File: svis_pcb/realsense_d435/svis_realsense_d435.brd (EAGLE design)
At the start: 57.1 x 41.3 mm, 14 parts, among them U1 MPU-6000QFN-24

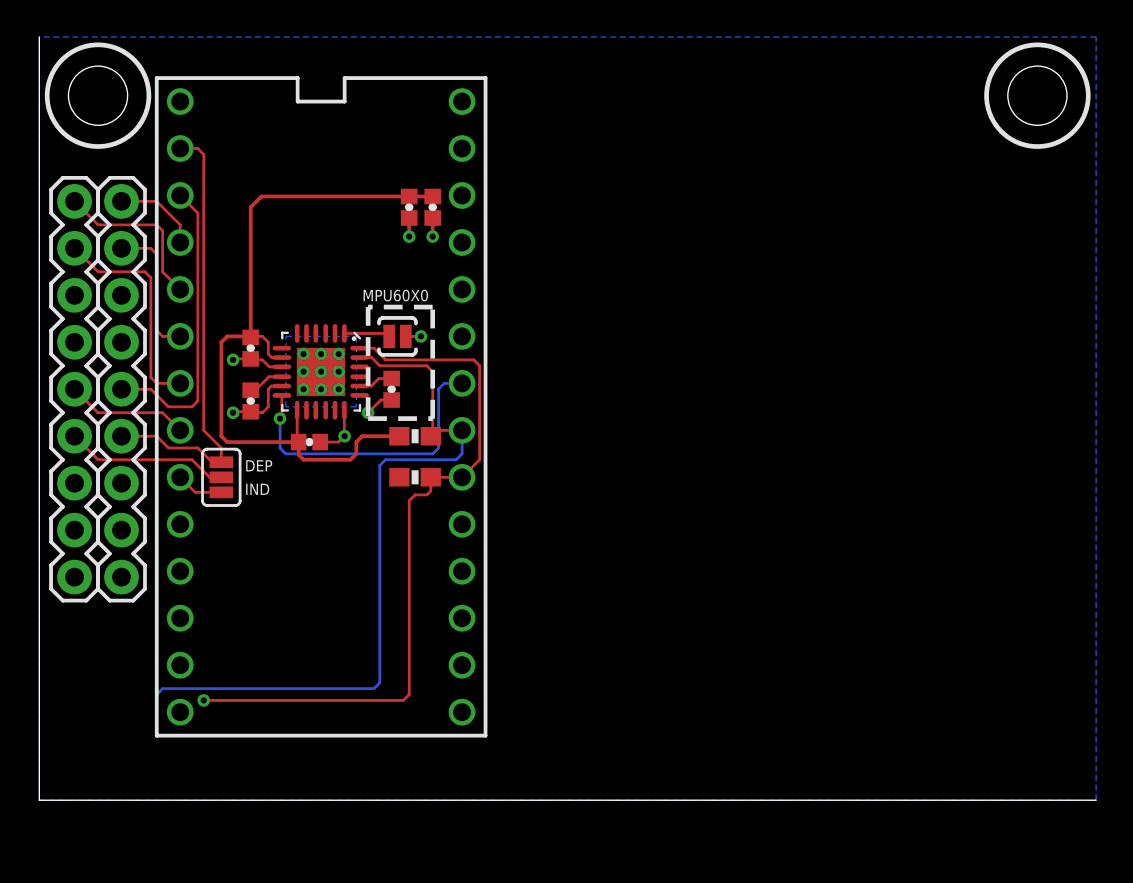
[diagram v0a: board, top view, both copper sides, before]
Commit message: Adding libraries and packages.
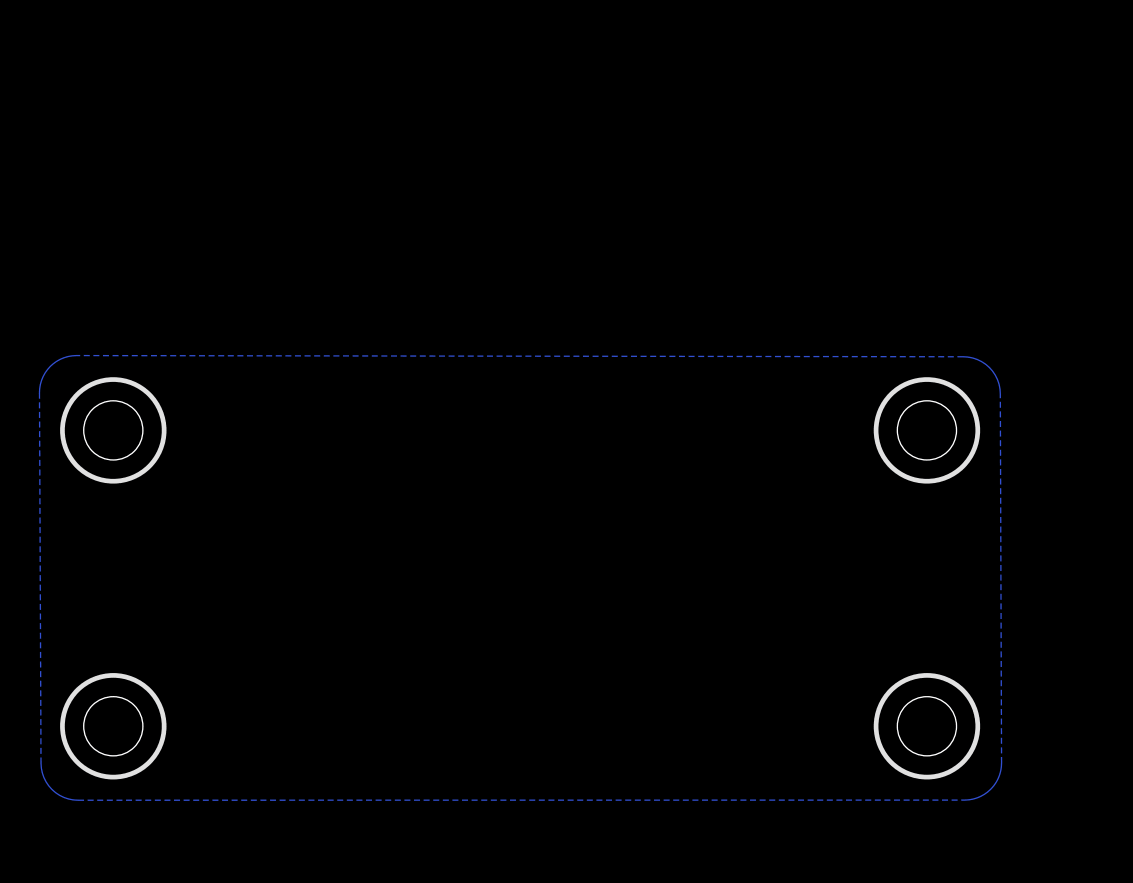
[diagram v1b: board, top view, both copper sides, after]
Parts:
- removed C1: DNP (2.2nF), SparkFun-Capacitors:0402-CAP
- removed C2, C3, C5, C6: 0.1uF, SparkFun-Capacitors:0402-CAP
- removed C4: 2.2uF, SparkFun-Capacitors:0402-CAP
- removed J2, J3: (no value), SparkFun-Connectors:1X09
- removed JP1: MPU6050, SparkFun-Passives:PAD-JUMPER-2-NO_YES_SILK
- removed JP2: JUMPER-SMT_3_NO_SILK, SparkFun-Jumpers:SMT-JUMPER_3_NO_SILK
- removed R1, R2: 4.7k, SparkFun-Resistors:0603-RES
- removed U$2: TEENSY_3.2, Teensy_3_and_LC_Series_Boards_v1.1:TEENSY3-DIL
- removed U1: MPU-6000QFN-24, SparkFun-Sensors:QFN-24-TESTING
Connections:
- removed net 3.3V: C3.1, C4.1, C5.1, C6.1, R1.2, R2.2, U$2.3.3V, U1.13, U1.8
- removed net C31_I0: J2.9, U$2.2
- removed net C31_IO2_RX: J2.5, U$2.1
- removed net C31_IO3_TX: J2.4, JP2.1, U$2.0
- removed net C31_O1: J2.8, U$2.4
- removed net C32_I0: J3.9, U$2.3
- removed net C32_IO2: J3.5, U$2.6
- removed net C32_IO3: J3.4, JP2.2
- removed net C32_IO3_T: JP2.3, U$2.7
- removed net C32_O1: J3.8, U$2.5
- removed net GND: C1.1, C2.1, C3.2, C4.2, C5.2, C6.2, J2.2, J2.6, J2.7, J3.2, J3.6, J3.7, JP1.1, U$2.AGND, U$2.GND, U1.11, U1.18, U1.9
- removed net IMU2_INT: U$2.20/A6, U1.12
- removed net N$7: C1.2, U1.20
- removed net N$8: JP1.2, U1.1
- removed net REGOUT: C2.2, U1.10
- removed net SCL: R1.1, U$2.19/A5, U1.23
- removed net SDA: R2.1, U$2.18/A4, U1.24
- removed net VIN: U$2.VIN
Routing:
- net 3.3V: track 39.8 -> 0.00 mm
- net SCL: track 39.6 -> 0.00 mm
- net SDA: track 38.8 -> 0.00 mm, vias 1 -> 0
- net C31_IO3_TX: track 24.4 -> 0.00 mm
- net IMU2_INT: track 16.3 -> 0.00 mm, vias 1 -> 0
- net C31_IO2_RX: track 16.2 -> 0.00 mm
- net GND: track 14.0 -> 0.00 mm, vias 7 -> 0
- net C32_O1: track 11.9 -> 0.00 mm
- net C32_I0: track 8.99 -> 0.00 mm
- net C32_IO3: track 8.86 -> 0.00 mm
- net C31_O1: track 7.57 -> 0.00 mm
- net C32_IO2: track 6.64 -> 0.00 mm
- net C31_I0: track 4.65 -> 0.00 mm
- net C32_IO3_T: track 2.56 -> 0.00 mm
- net N$8: track 2.49 -> 0.00 mm
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- removed copper zone on layer 16, net HS
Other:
- board outline removed
- board text removed: "DEP"
- board text removed: "IND"
- board text removed: "MPU60X0"

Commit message: WIP.
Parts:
- added C1: 0.1uF, SparkFun-Capacitors:0402
- added U$1: TEENSY_3.0_DIL, teensy:TEENSY_3.0-3.2&LC_DIL
- added U1: ICM-20689, svis:QFN50P400X400X95-25N
- added U2: SM09B-SRSS-TB, svis:SM09B-SRSS-TB
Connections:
- new net 3.3V: U$1.3.3V, U1.13, U1.8
- new net GND: C1.1, U$1.AGND, U$1.GND, U1.11, U1.18, U1.25
- new net IMU_INT: U1.12
- new net N$1: C1.2, U1.10
- new net VIN: U$1.VIN

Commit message: First cut at complete board.
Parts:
- added C2: 0.1uF, SparkFun-Capacitors:0603
- added C3: 2.2uF, SparkFun-Capacitors:0603
- added C4: 10nF, SparkFun-Capacitors:0603
- added CAM2: SM09B-SRSS-TB, svis:SM09B-SRSS-TB
- added R1, R2: 4.7k, SparkFun-Resistors:0603
- C1: value 0.1uF -> 0.47uF; device SparkFun-Capacitors:0402 -> SparkFun-Capacitors:0603
- moved C1 24.0 mm to (24.0, 7.50), flipped to the bottom
- renumbered U$1 to TEENSY, U1 to ICM20689, U2 to CAM1
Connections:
- new net CAM1_GND: CAM1.9
- new net CAM1_IO: CAM1.1, TEENSY.3
- new net CAM1_RX: CAM1.7, TEENSY.1
- new net CAM1_STROBE: CAM1.5, TEENSY.4
- new net CAM1_TRIGGER: CAM1.3, TEENSY.2
- new net CAM1_TX: CAM1.8, TEENSY.0
- new net CAM2_GND: CAM2.9
- new net CAM2_IO: CAM2.1, TEENSY.7
- new net CAM2_RX: CAM2.7, TEENSY.10
- new net CAM2_STROBE: CAM2.5, TEENSY.8
- new net CAM2_TRIGGER: CAM2.3, TEENSY.6
- new net CAM2_TX: CAM2.8, TEENSY.9
- new net IMU_SCL: ICM20689.23, R1.1, TEENSY.19/A5
- new net IMU_SDA: ICM20689.24, R2.1, TEENSY.18/A4
- new net N$2: C2.2, C3.2, ICM20689.13
- net 3.3V: now also C2.1, C3.1, C4.2, ICM20689.22, R1.2, R2.2; no longer ICM20689.13
- net GND: now also C1.2, C4.1, CAM1.2, CAM1.4, CAM1.6, CAM2.2, CAM2.4, CAM2.6, ICM20689.9; no longer C1.1
- net IMU_INT: now also TEENSY.20/A6
- net N$1: now also C1.1; no longer C1.2
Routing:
- net GND: track 0.00 -> 75.1 mm
- net 3.3V: track 0.00 -> 41.6 mm, vias 0 -> 2
- net IMU_SCL: track 0.00 -> 22.5 mm
- net CAM2_IO: track 0.00 -> 16.3 mm, vias 0 -> 1
- net CAM2_TRIGGER: track 0.00 -> 16.2 mm, vias 0 -> 1
- net N$2: track 0.00 -> 14.3 mm
- net IMU_INT: track 0.00 -> 13.3 mm
- net CAM1_TX: track 0.00 -> 12.8 mm, vias 0 -> 1
- net CAM1_STROBE: track 0.00 -> 12.8 mm, vias 0 -> 1
- net CAM2_TX: track 0.00 -> 12.6 mm, vias 0 -> 2
- net IMU_SDA: track 0.00 -> 12.2 mm, vias 0 -> 1
- net CAM1_IO: track 0.00 -> 12.0 mm
- net CAM2_STROBE: track 0.00 -> 11.5 mm, vias 0 -> 1
- net CAM1_RX: track 0.00 -> 11.3 mm, vias 0 -> 1
- net CAM1_TRIGGER: track 0.00 -> 8.99 mm, vias 0 -> 1
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
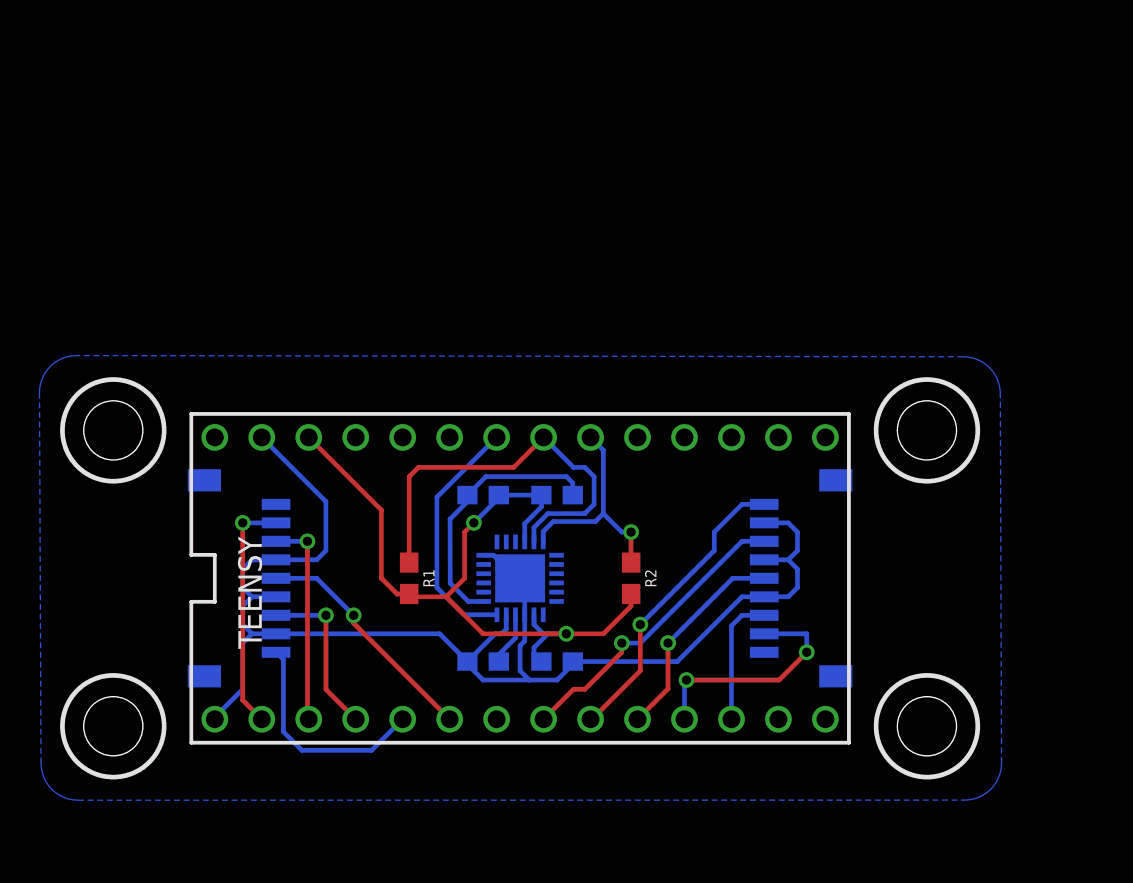
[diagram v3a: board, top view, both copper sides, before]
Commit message: Add ground plane.
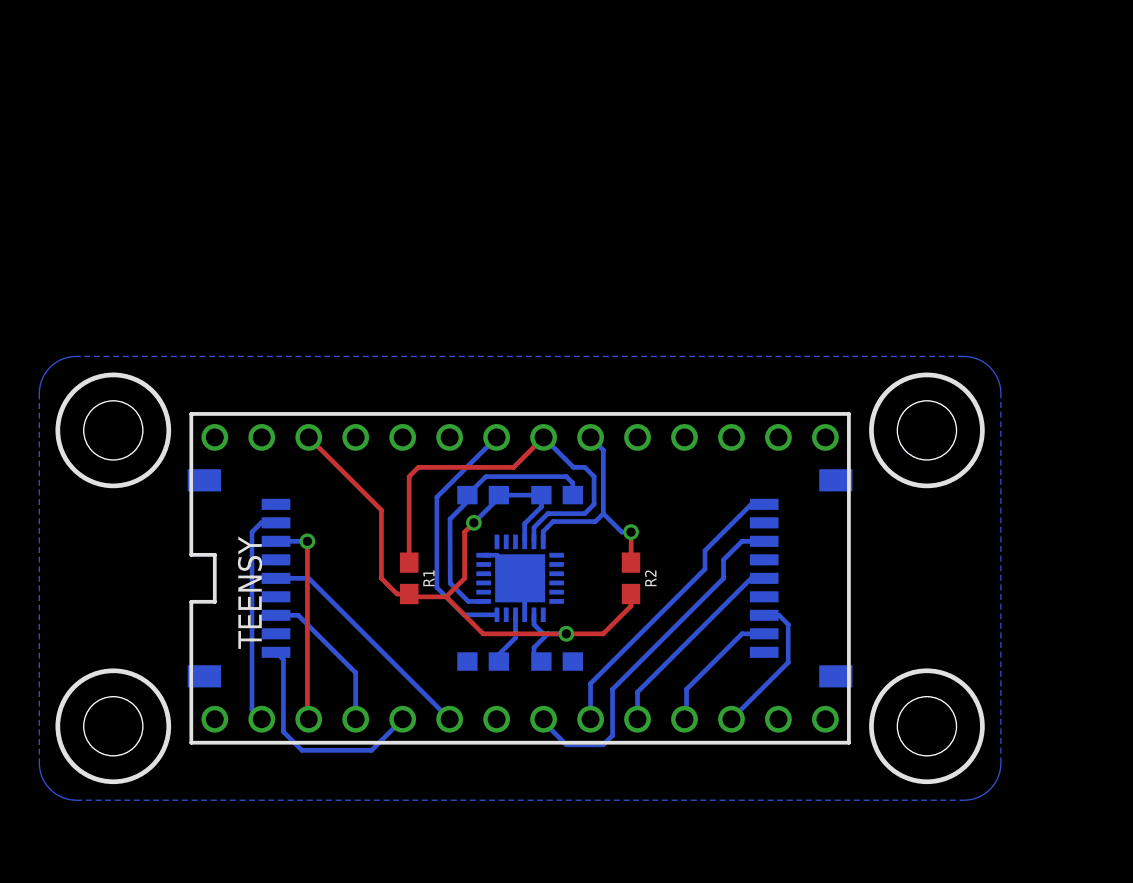
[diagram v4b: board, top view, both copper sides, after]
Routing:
- net GND: track 75.1 -> 4.56 mm
- net CAM2_TX: track 12.6 -> 7.11 mm, vias 2 -> 0
- net CAM2_TRIGGER: track 16.2 -> 19.2 mm, vias 1 -> 0
- net CAM1_TX: track 12.8 -> 11.8 mm, vias 1 -> 0
- net CAM1_TRIGGER: track 8.99 -> 8.11 mm, vias 1 -> 0
- net CAM2_RX: track 7.06 -> 7.90 mm
- net CAM2_STROBE: track 11.5 -> 10.9 mm, vias 1 -> 0
- net CAM2_IO: track 16.3 -> 15.9 mm, vias 1 -> 0
- net CAM1_STROBE: track 12.8 -> 12.5 mm, vias 1 -> 0

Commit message: Update design to pass DRC and ERC.
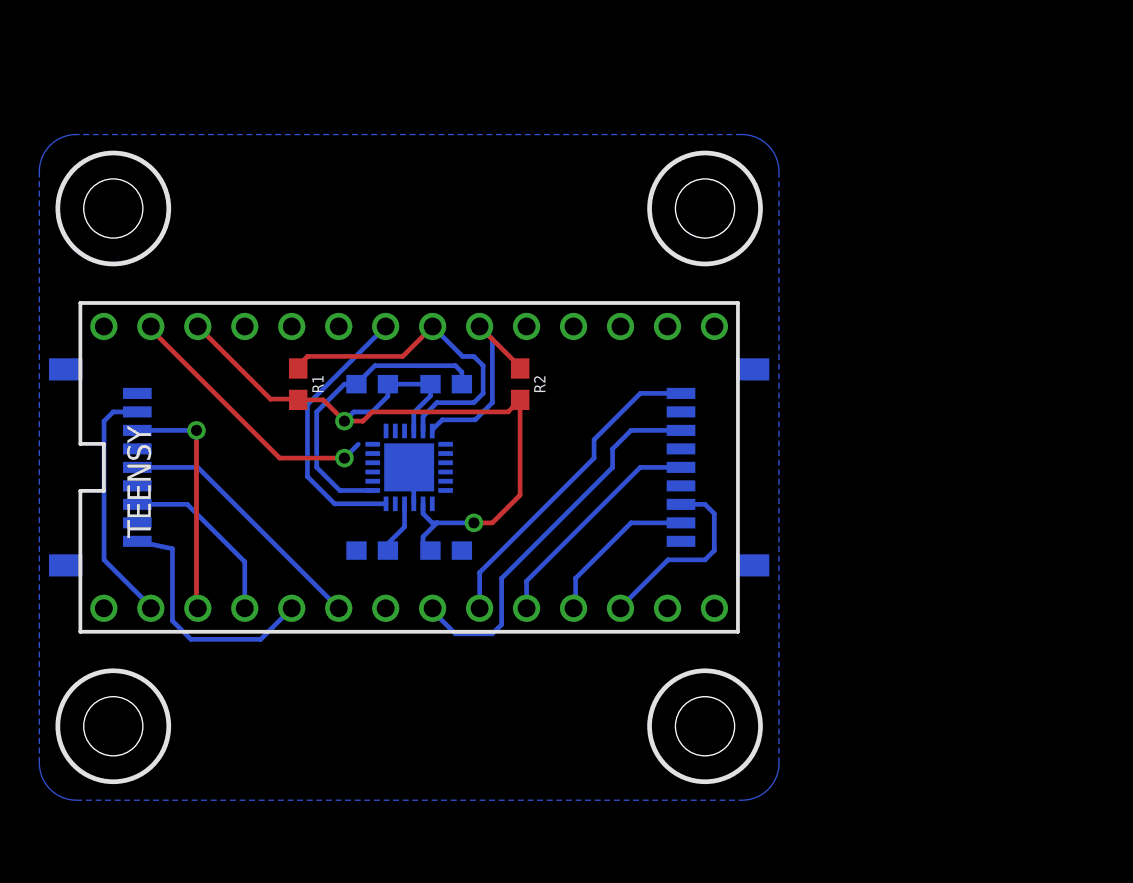
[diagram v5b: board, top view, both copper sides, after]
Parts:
- moved R1 12.1 mm to (14.0, 22.5)
- moved R2 12.1 mm to (26.0, 22.5)
- moved CAM1 9.60 mm to (5.30, 16.5)
- moved C1 8.49 mm to (18.0, 13.5)
- moved C2 8.49 mm to (18.0, 22.5)
- moved C3 8.49 mm to (22.0, 22.5)
- moved C4 8.49 mm to (22.0, 13.5)
- moved ICM20689 8.49 mm to (20.0, 18.0)
- moved TEENSY 8.49 mm to (20.0, 18.0)
- moved CAM2 7.50 mm to (34.7, 19.5)
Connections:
- removed net CAM1_GND: CAM1.9
- removed net CAM2_GND: CAM2.9
- net GND: now also CAM1.9, CAM2.9
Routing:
- net GND: track 4.56 -> 15.6 mm, vias 0 -> 1
- net IMU_SCL: track 22.5 -> 18.0 mm
- net CAM2_RX: track 7.90 -> 10.4 mm
- net N$2: track 14.3 -> 16.2 mm
- net CAM1_TRIGGER: track 8.11 -> 9.61 mm
- net CAM1_STROBE: track 12.5 -> 14.0 mm
- net CAM2_TRIGGER: track 19.2 -> 20.7 mm
- net CAM2_STROBE: track 10.9 -> 12.4 mm
- net CAM2_TX: track 7.11 -> 8.61 mm
- net CAM2_IO: track 15.9 -> 17.4 mm
- net CAM1_RX: track 11.3 -> 12.8 mm
- net IMU_INT: track 13.3 -> 14.7 mm
- net CAM1_IO: track 12.0 -> 13.4 mm
- net CAM1_TX: track 11.8 -> 13.2 mm
- net 3.3V: track 41.6 -> 42.7 mm
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
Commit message: Incorporate Samir's comments
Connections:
- removed net N$2: C2.2, C3.2, ICM20689.13
- net 3.3V: now also ICM20689.13
- net GND: now also C2.2, C3.2
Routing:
- net N$2: track 16.2 -> 0.00 mm
- net 3.3V: track 42.7 -> 48.1 mm
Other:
- board text added: "--> X"
- board text added: "--> Y"
- board text added: "Y <--"
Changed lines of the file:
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@@
 <hole x="36" y="4" drill="3.2"/>
 <circle x="36" y="4" radius="3" width="0.254" layer="21"/>
+<text x="31" y="1.5" size="1.778" layer="16" rot="MR0">Y &lt;--</text>
+<text x="31" y="1.5" size="1.778" layer="16" rot="MR0">Y &lt;--</text>
+<text x="28.5" y="18.5" size="1.778" layer="16" rot="MR0">Y &lt;--</text>
+<text x="30" y="4.5" size="1.778" layer="16" rot="MR0">Y &lt;--</text>
+<text x="26" y="2" size="1.778" layer="16" rot="MR0">Y &lt;--</text>
+<text x="26.5" y="0.5" size="1.778" layer="16" rot="MR0">Y &lt;--</text>
+<text x="31.5" y="1.5" size="1.778" layer="26" rot="MR0">Y &lt;--</text>
+<text x="25" y="2.5" size="1.778" layer="26" rot="MR90">--&gt; X</text>
+<text x="31" y="28.5" size="1.778" layer="16" rot="MR0">Y &lt;--</text>
+<text x="31" y="28.5" size="1.778" layer="16" rot="MR0">Y &lt;--</text>
+<text x="30" y="31.5" size="1.778" layer="16" rot="MR0">Y &lt;--</text>
+<text x="26" y="29" size="1.778" layer="16" rot="MR0">Y &lt;--</text>
+<text x="31.5" y="28.5" size="1.778" layer="26" rot="MR0">Y &lt;--</text>
+<text x="25" y="29.5" size="1.778" layer="26" rot="MR90">--&gt; X</text>
+<text x="12.5" y="28.5" size="1.778" layer="25">--&gt; Y</text>
+<text x="12.5" y="1.5" size="1.778" layer="25">--&gt; Y</text>
+<text x="13" y="2.5" size="1.778" layer="25" rot="R90">--&gt; X</text>
+<text x="13" y="29.5" size="1.778" layer="25" rot="R90">--&gt; X</text>
 </plain>
 <attributes>
@@
 <wire x1="6.03" y1="25.47" x2="13" y2="18.5" width="0.254" layer="1"/>
 <wire x1="13" y1="18.5" x2="16.5" y2="18.5" width="0.254" layer="1"/>
+<contactref element="C2" pad="2"/>
+<contactref element="C3" pad="2"/>
 </signal>
 <signal name="3.3V">
@@
 <contactref element="R1" pad="2"/>
 <contactref element="R2" pad="2"/>
-<contactref element="C3" pad="1"/>
-<contactref element="C2" pad="1"/>
 <contactref element="ICM20689" pad="8"/>
 <contactref element="C4" pad="2"/>
 <contactref element="ICM20689" pad="22"/>
 <wire x1="12.5" y1="21.69" x2="8.57" y2="25.62" width="0.254" layer="1"/>
-<wire x1="21.15" y1="22.5" x2="21.15" y2="21.86" width="0.254" layer="16"/>
 <wire x1="21.15" y1="21.86" x2="20.25" y2="20.96" width="0.254" layer="16"/>
 <wire x1="20.25" y1="20.96" x2="20.25" y2="19.97" width="0.254" layer="16"/>
-<wire x1="18.85" y1="22.5" x2="21.15" y2="22.5" width="0.254" layer="16"/>
-<wire x1="18.85" y1="22.5" x2="18.85" y2="22.35" width="0.254" layer="16"/>
 <via x="16.5" y="20.5" extent="1-16" drill="0.6"/>
 <wire x1="26" y1="21.65" x2="26" y2="16.5" width="0.254" layer="1"/>
@@
 <wire x1="25.35" y1="21" x2="26" y2="21.65" width="0.254" layer="1"/>
 <wire x1="25.35" y1="21" x2="18" y2="21" width="0.254" layer="1"/>
-<wire x1="18.85" y1="21.85" x2="18.85" y2="22.5" width="0.254" layer="16"/>
 <wire x1="14" y1="21.65" x2="15.35" y2="21.65" width="0.254" layer="1"/>
 <wire x1="15.35" y1="21.65" x2="16.5" y2="20.5" width="0.254" layer="1"/>
@@
 <wire x1="17" y1="21" x2="18" y2="21" width="0.254" layer="16"/>
 <wire x1="18" y1="21" x2="18.85" y2="21.85" width="0.254" layer="16"/>
+<contactref element="C3" pad="1"/>
+<contactref element="C2" pad="1"/>
+<wire x1="18.85" y1="22.5" x2="21.15" y2="22.5" width="0.254" layer="16"/>
+<wire x1="18.85" y1="22.5" x2="18.85" y2="22.35" width="0.254" layer="16"/>
+<contactref element="ICM20689" pad="13"/>
+<wire x1="18.03" y1="16.75" x2="16.25" y2="16.75" width="0.254" layer="16"/>
+<wire x1="16.25" y1="16.75" x2="15" y2="18" width="0.254" layer="16"/>
+<wire x1="15" y1="19" x2="16.5" y2="20.5" width="0.254" layer="16"/>
+<wire x1="15" y1="19" x2="15" y2="18" width="0.254" layer="16"/>
+<wire x1="18.85" y1="21.85" x2="18.85" y2="22.35" width="0" layer="19" extent="16-16"/>
+<wire x1="21.15" y1="21.86" x2="21.15" y2="22.5" width="0" layer="19" extent="16-16"/>
 </signal>
 <signal name="VIN">
@@
 <wire x1="22.89" y1="24" x2="21.27" y2="25.62" width="0.254" layer="16"/>
 </signal>
-<signal name="N$2">
-<contactref element="ICM20689" pad="13"/>
-<contactref element="C3" pad="2"/>
-<contactref element="C2" pad="2"/>
-<wire x1="22.85" y1="22.5" x2="22.85" y2="23.15" width="0.254" layer="16"/>
-<wire x1="22.85" y1="23.15" x2="22.5" y2="23.5" width="0.254" layer="16"/>
-<wire x1="22.5" y1="23.5" x2="18.15" y2="23.5" width="0.254" layer="16"/>
-<wire x1="18.15" y1="23.5" x2="17.15" y2="22.5" width="0.254" layer="16"/>
-<wire x1="15" y1="18" x2="16.25" y2="16.75" width="0.254" layer="16"/>
-<wire x1="16.25" y1="16.75" x2="18.03" y2="16.75" width="0.254" layer="16"/>
-<wire x1="15" y1="21" x2="16.5" y2="22.5" width="0.254" layer="16"/>
-<wire x1="16.5" y1="22.5" x2="17.15" y2="22.5" width="0.254" layer="16"/>
-<wire x1="15" y1="18" x2="15" y2="21" width="0.254" layer="16"/>
-</signal>
 <signal name="N$1">
